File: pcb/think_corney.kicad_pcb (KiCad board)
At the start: 2 copper layers, 130.3 x 86.5 mm, 112 parts

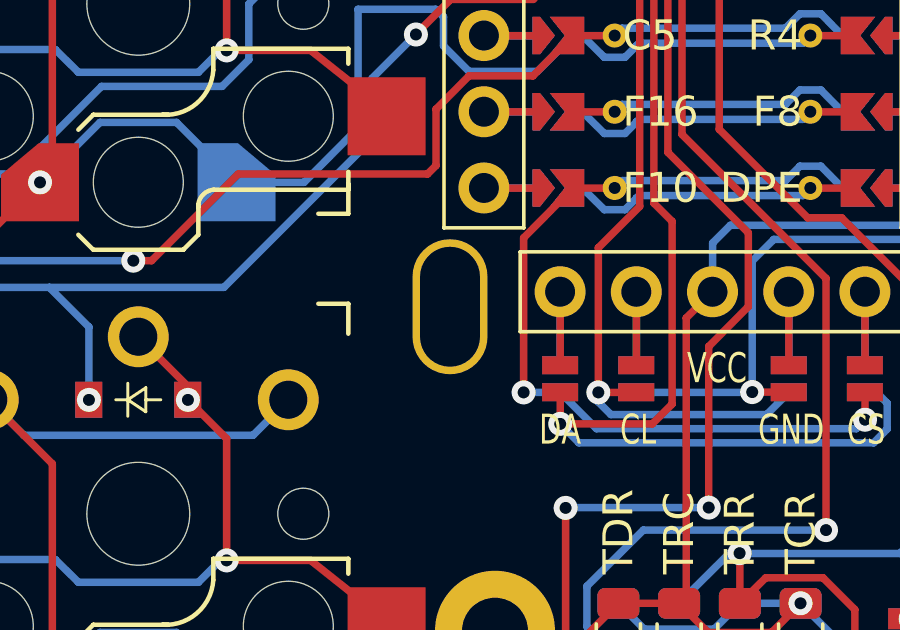
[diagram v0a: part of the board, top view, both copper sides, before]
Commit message: Ergogen: Increase battery hole size
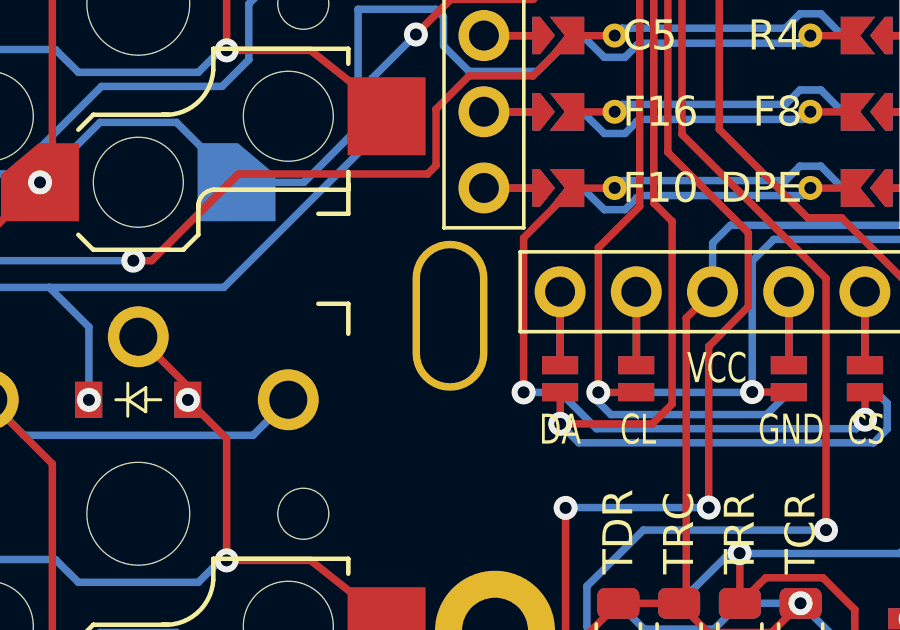
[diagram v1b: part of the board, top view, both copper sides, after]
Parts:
- moved H1 0.30 mm to (199.3, 82.3)
- moved P34" 0.30 mm to (199.3, 82.3)

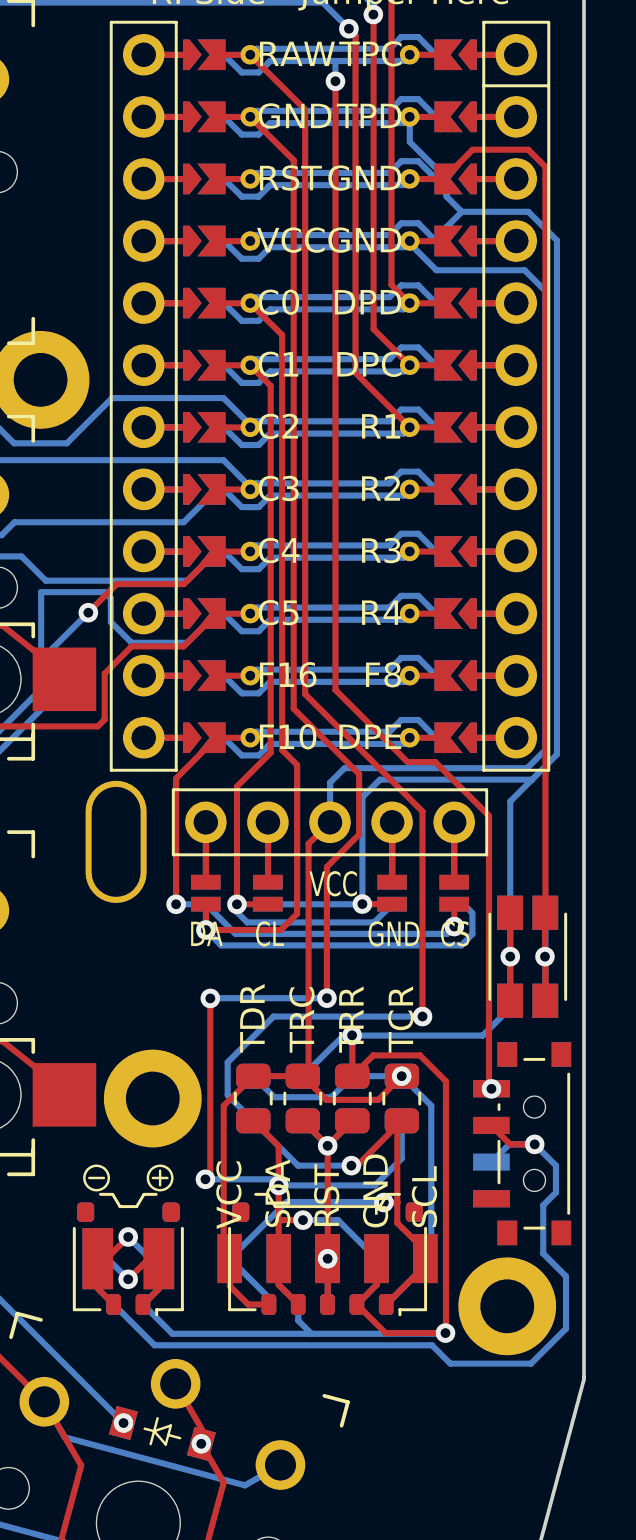
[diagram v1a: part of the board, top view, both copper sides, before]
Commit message: Ergogen: Moved reset switch closer to board edge
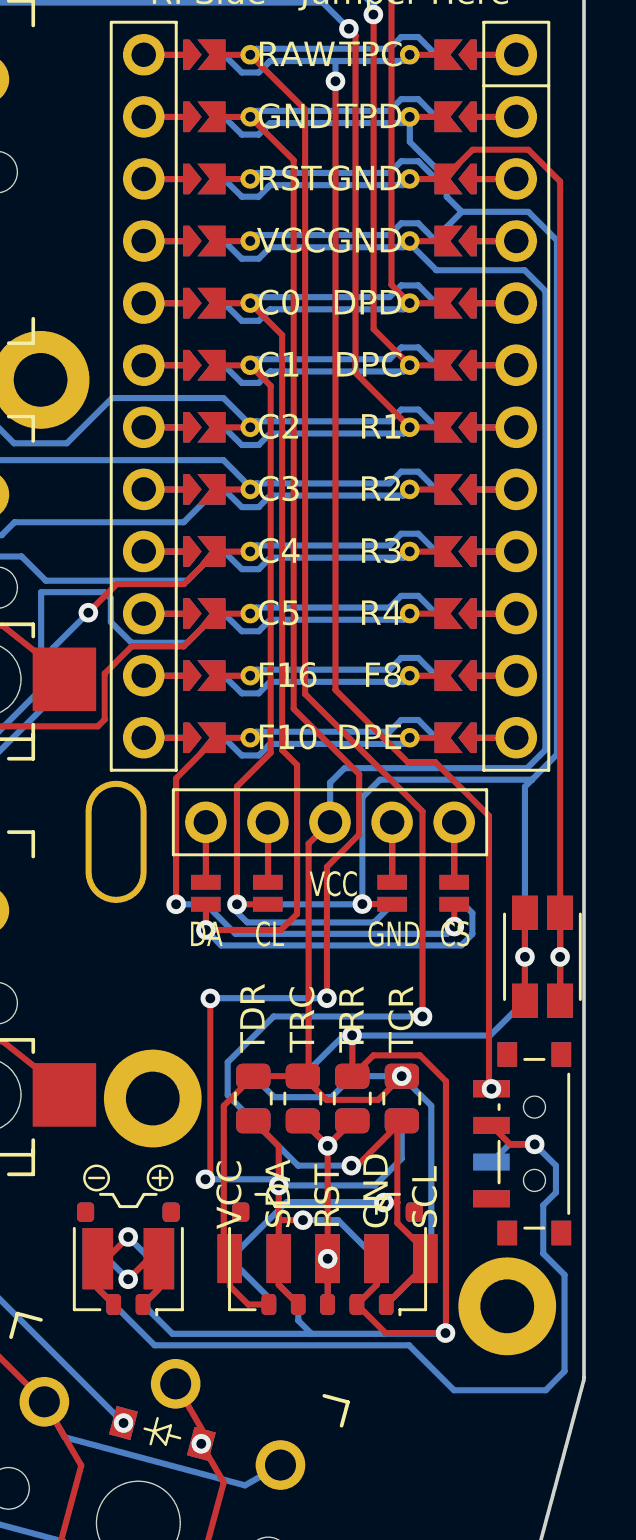
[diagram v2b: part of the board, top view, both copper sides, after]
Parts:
- moved P38" 0.60 mm to (216.7, 87.0)
- moved SW2 0.60 mm to (216.7, 87.0)
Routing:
- net BAT_P: track 37.0 -> 38.8 mm
- net GND: track 147.9 -> 147.0 mm
